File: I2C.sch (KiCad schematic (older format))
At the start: 17 parts, among them J5 Grove, J6 Grove, J7 Conn_01x04_Male, U8 LM75B, U9 STC3100

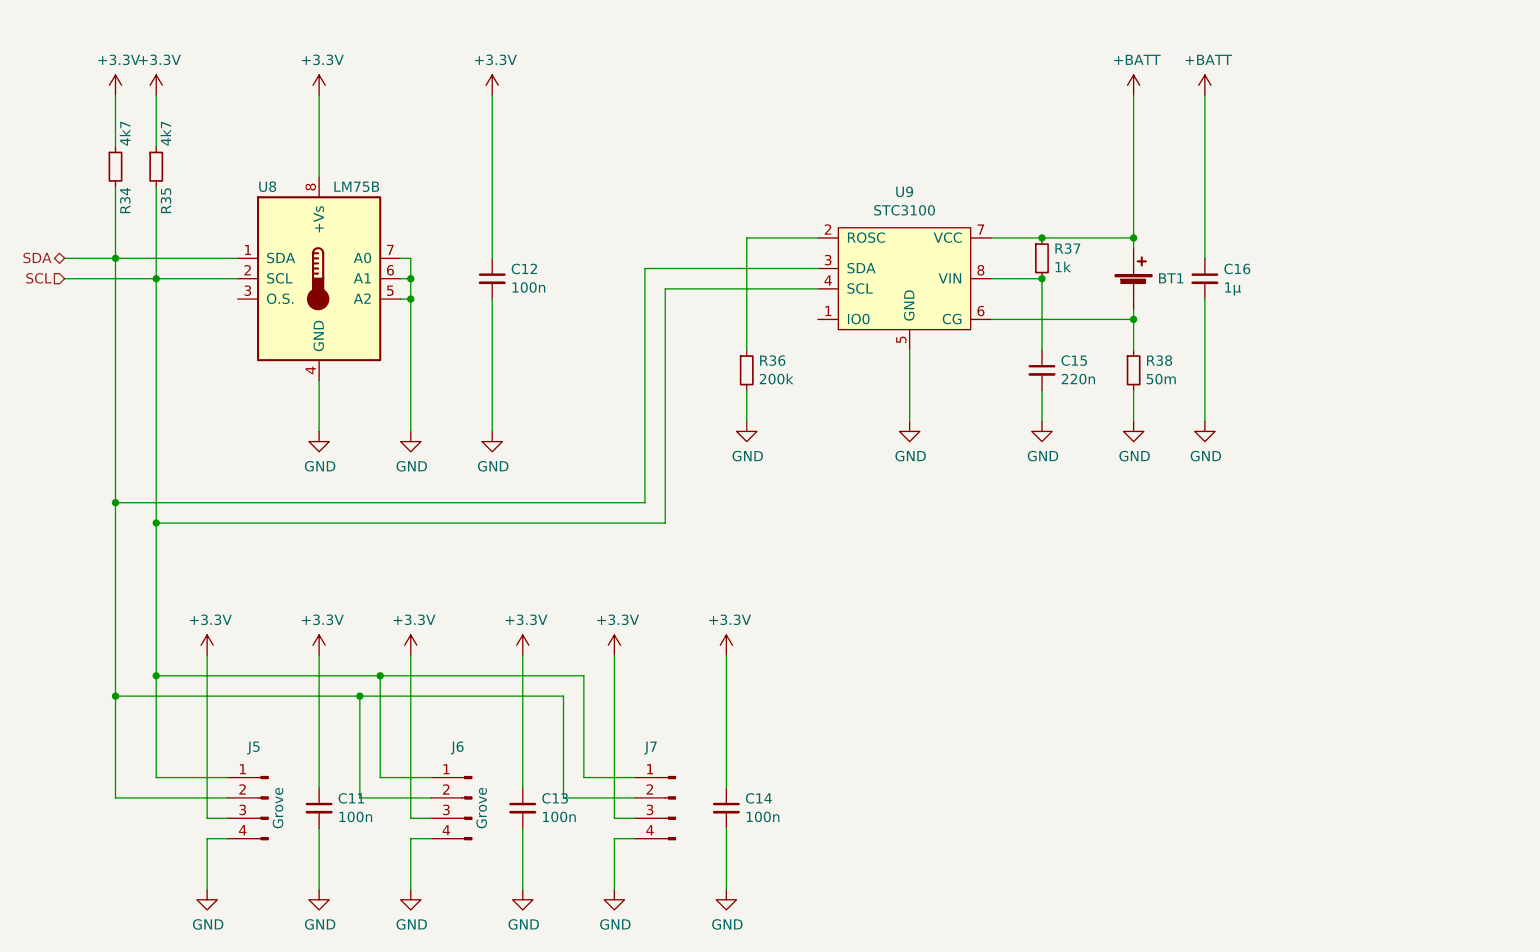
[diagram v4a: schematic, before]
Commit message: LM75 durch TMP411 ersetzt
-Temperatursensor getauscht
-3,3V 2mm Buchse hinzugeügt
-Bohrlöcher wieder eingefügt
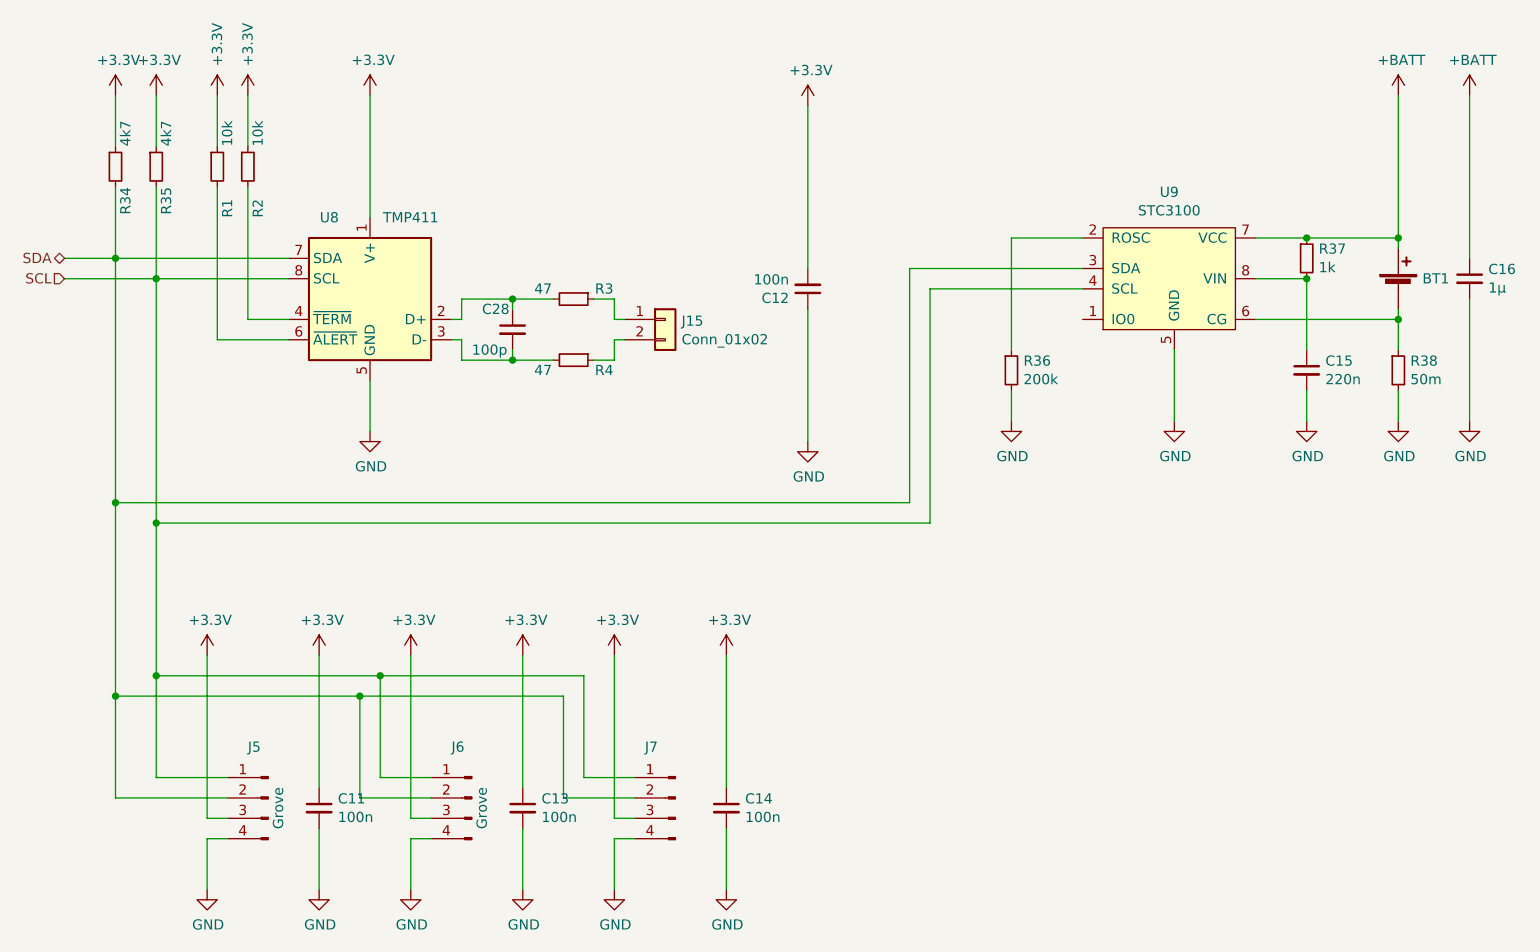
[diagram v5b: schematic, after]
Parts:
- removed U8: LM75B, Package_SO:SO-8_3.9x4.9mm_P1.27mm, symbol MCT_Labor_5529-rescue:LM75B-Sensor_Temperature
- added C28: 100p, Capacitor_SMD:C_0603_1608Metric_Pad1.05x0.95mm_HandSolder, symbol Device:C_Small
- added J15: Conn_01x02, Connector_PinHeader_2.54mm:PinHeader_1x02_P2.54mm_Vertical, symbol Connector_Generic:Conn_01x02
- added R1, R2: 10k, Resistor_SMD:R_0603_1608Metric_Pad1.05x0.95mm_HandSolder, symbol Device:R_Small
- added R3, R4: 47, Resistor_SMD:R_0603_1608Metric_Pad1.05x0.95mm_HandSolder, symbol Device:R_Small
- added U8: TMP411, Package_SO:SO-8_3.9x4.9mm_P1.27mm, symbol Sensor_Temperature:TMP411
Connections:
- net +3V3: now also C12.2, R1.1, R2.1, U8.1 (V+); no longer C12.1
- net GND: now also C12.1, U8.5 (GND); no longer C12.2
- net SCL: now also U8.8 (SCL)
- net SDA: now also U8.7 (SDA)
- new net: C28.1, R3.2, U8.2 (D+)
- new net: C28.2, R4.2, U8.3 (D-)
- new net: R2.2, U8.4 (~TERM)
- new net: R1.2, U8.6 (~ALERT)
- new net: J15.1 (Pin_1), R3.1
- new net: J15.2 (Pin_2), R4.1
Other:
- moved on the sheet: BT1, C12, C15, C16, R36, R37, R38, U9

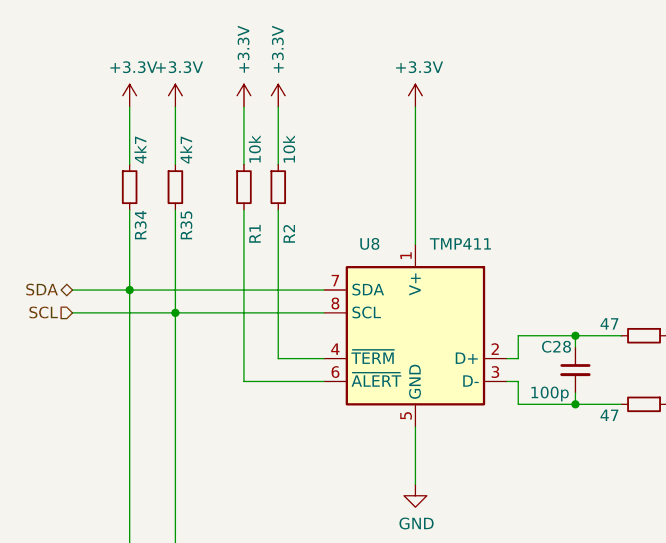
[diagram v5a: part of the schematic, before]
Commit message: LEDs beim TMP411 hinzugegfügt
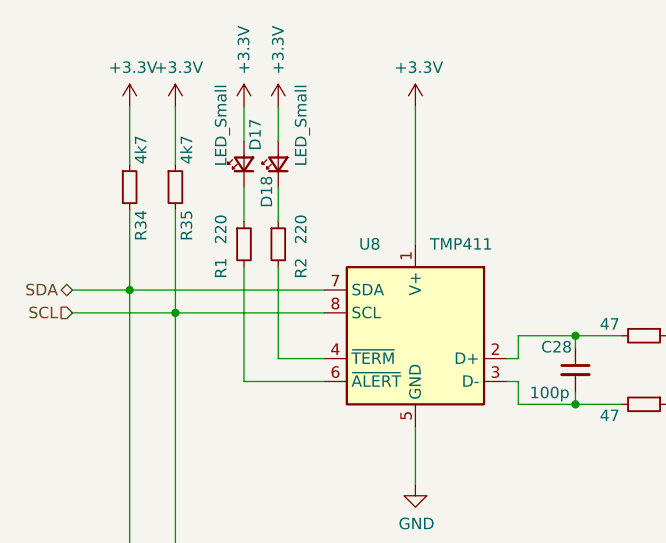
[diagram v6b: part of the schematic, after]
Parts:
- added D17, D18: LED_Small, LED_SMD:LED_0603_1608Metric_Pad1.05x0.95mm_HandSolder, symbol Device:LED_Small
- R1, R2: value 10k -> 220
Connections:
- net +3V3: now also D17.2 (A), D18.2 (A); no longer R1.1, R2.1
- new net: D17.1 (K), R1.1
- new net: D18.1 (K), R2.1
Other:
- moved on the sheet: R1, R2
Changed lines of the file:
@@
-$EndComp
-$Comp
-L Device:R_Small R1
-U 1 1 5F2CDCBC
-P 2950 1800
-F 0 "R1" V 3000 1550 50  0000 L CNN
-F 1 "10k" V 3000 1900 50  0000 L CNN
-F 2 "Resistor_SMD:R_0603_1608Metric_Pad1.05x0.95mm_HandSolder" H 2950 1800 50  0001 C CNN
-F 3 "~" H 2950 1800 50  0001 C CNN
-	1    2950 1800
-	1    0    0    -1
 $EndComp
 $Comp
 L Device:R_Small R2
 U 1 1 5F2CE365
-P 3100 1800
-F 0 "R2" V 3150 1550 50  0000 L CNN
-F 1 "10k" V 3150 1900 50  0000 L CNN
-F 2 "Resistor_SMD:R_0603_1608Metric_Pad1.05x0.95mm_HandSolder" H 3100 1800 50  0001 C CNN
-F 3 "~" H 3100 1800 50  0001 C CNN
-	1    3100 1800
+P 3100 2050
+F 0 "R2" V 3200 1900 50  0000 L CNN
+F 1 "220" V 3200 2050 50  0000 L CNN
+F 2 "Resistor_SMD:R_0603_1608Metric_Pad1.05x0.95mm_HandSolder" H 3100 2050 50  0001 C CNN
+F 3 "~" H 3100 2050 50  0001 C CNN
+	1    3100 2050
 	1    0    0    -1
 $EndComp
@@
 	2650 2350 3300 2350
 Wire Wire Line
-	2950 1450 2950 1700
-Wire Wire Line
-	3100 1450 3100 1700
-Wire Wire Line
-	2950 1900 2950 2650
-Wire Wire Line
 	2950 2650 3300 2650
-Wire Wire Line
-	3100 1900 3100 2550
 Wire Wire Line
 	3100 2550 3300 2550
@@
 Wire Wire Line
 	4900 2650 4950 2650
+$Comp
+L Device:R_Small R1
+U 1 1 5F2CDCBC
+P 2950 2050
+F 0 "R1" V 2850 1900 50  0000 L CNN
+F 1 "220" V 2850 2050 50  0000 L CNN
+F 2 "Resistor_SMD:R_0603_1608Metric_Pad1.05x0.95mm_HandSolder" H 2950 2050 50  0001 C CNN
+F 3 "~" H 2950 2050 50  0001 C CNN
+	1    2950 2050
+	1    0    0    -1
+$EndComp
+Wire Wire Line
+	2950 2150 2950 2650
+Wire Wire Line
+	3100 2150 3100 2550
+$Comp
+L Device:LED_Small D17
+U 1 1 5F2B74E8
+P 2950 1700
+F 0 "D17" H 3150 1650 50  0000 R CNN
+F 1 "LED_Small" H 3300 1800 50  0000 R CNN
+F 2 "LED_SMD:LED_0603_1608Metric_Pad1.05x0.95mm_HandSolder" V 2950 1700 50  0001 C CNN
+F 3 "~" V 2950 1700 50  0001 C CNN
+	1    2950 1700
+	0    -1   -1   0
+$EndComp
+$Comp
+L Device:LED_Small D18
+U 1 1 5F2B887E
+P 3100 1700
+F 0 "D18" H 3050 1750 50  0000 R CNN
+F 1 "LED_Small" H 3450 1600 50  0000 R CNN
+F 2 "LED_SMD:LED_0603_1608Metric_Pad1.05x0.95mm_HandSolder" V 3100 1700 50  0001 C CNN
+F 3 "~" V 3100 1700 50  0001 C CNN
+	1    3100 1700
+	0    -1   -1   0
+$EndComp
+Wire Wire Line
+	2950 1450 2950 1600
+Wire Wire Line
+	3100 1450 3100 1600
+Wire Wire Line
+	2950 1800 2950 1950
+Wire Wire Line
+	3100 1800 3100 1950
 $EndSCHEMATC

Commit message: Aktuell gefertigte Variante
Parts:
- C15: value 220n -> 100n
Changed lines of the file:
@@
 P 8300 2800
 F 0 "C15" H 8392 2846 50  0000 L CNN
-F 1 "220n" H 8392 2755 50  0000 L CNN
+F 1 "100n" H 8392 2755 50  0000 L CNN
 F 2 "Capacitor_SMD:C_0603_1608Metric_Pad1.05x0.95mm_HandSolder" H 8300 2800 50  0001 C CNN
 F 3 "~" H 8300 2800 50  0001 C CNN
